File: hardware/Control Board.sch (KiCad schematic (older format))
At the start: 38 parts, among them J1 Conn_FTDI, J2 SOLAR, M1 Motor_DC, Q1 IRF7105PbF, Q2 BC817W, Q3 BC817W, Q4 IRF7105PbF, SW1 SW_Push, SW2 SW_Push, SW3 SW_Push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

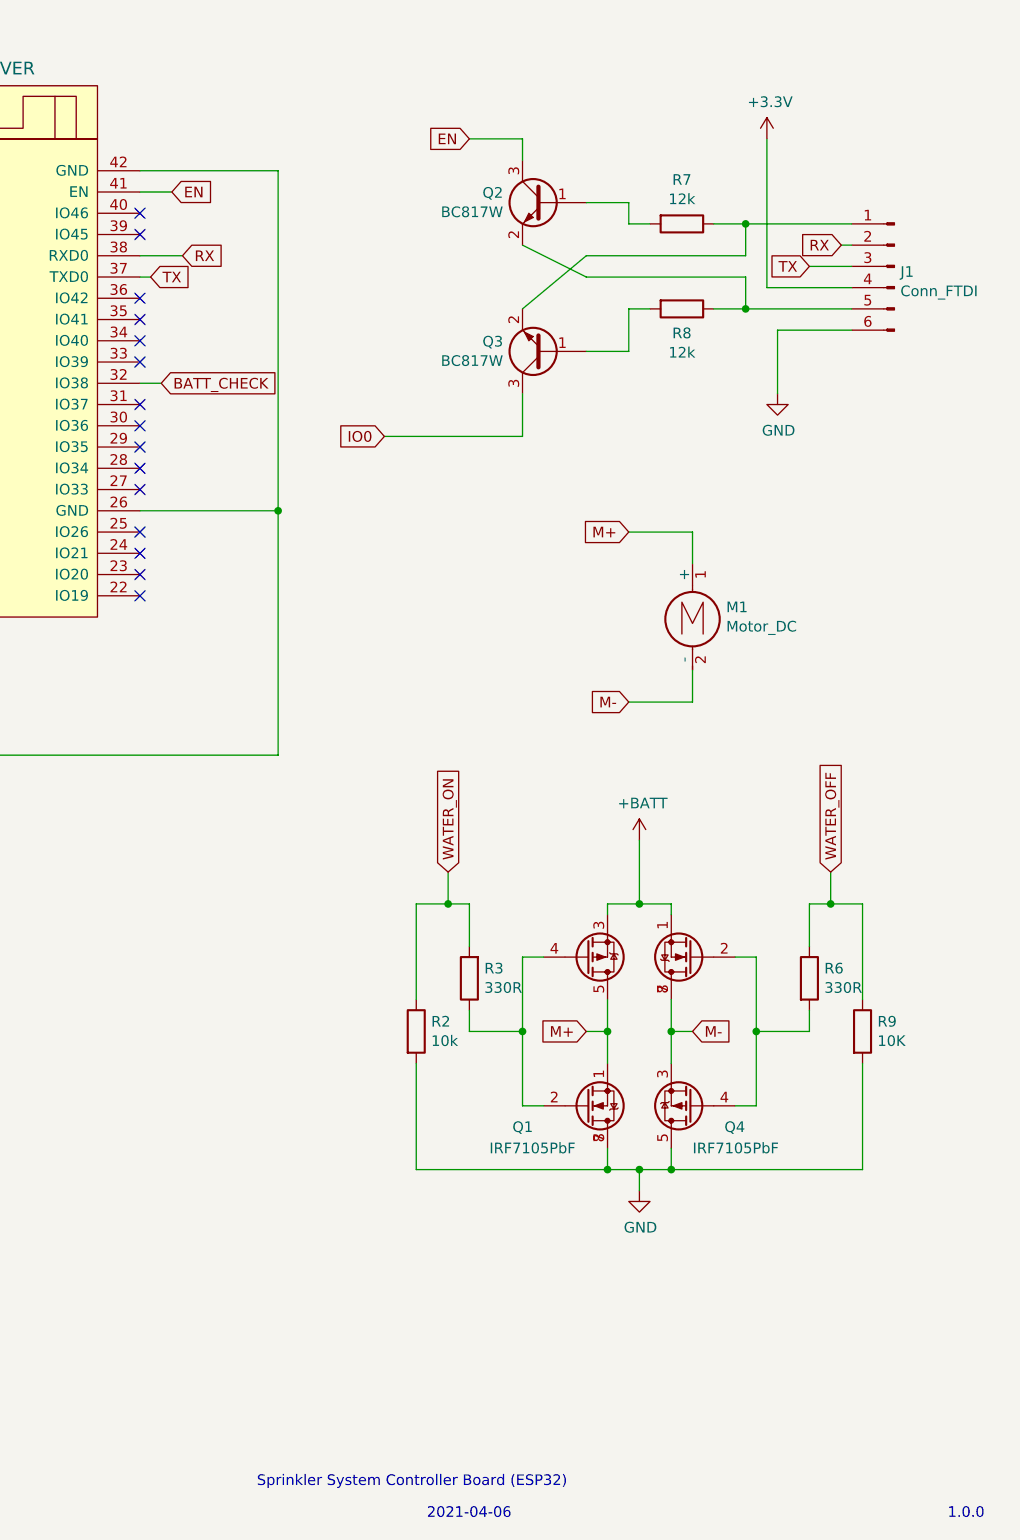
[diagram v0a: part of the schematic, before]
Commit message: Add pull up resistors on the auto programmer circuit, switch the RX and TX lines
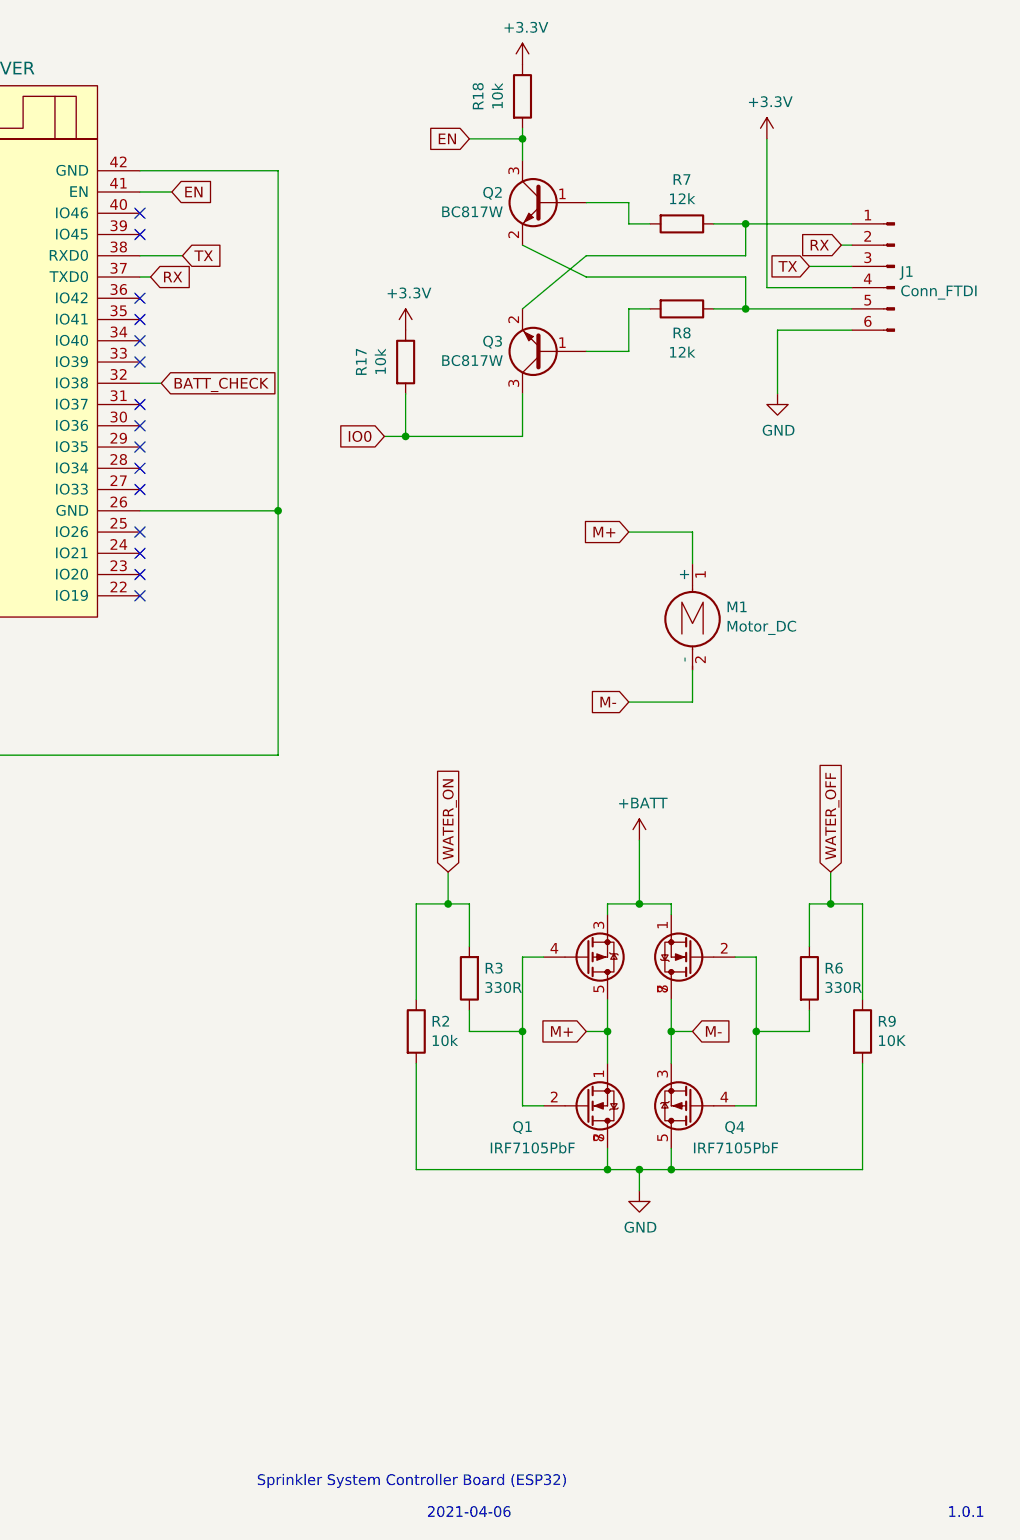
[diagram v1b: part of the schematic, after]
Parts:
- added R17, R18: 10k, Resistor_SMD:R_0402_1005Metric, symbol Device:R
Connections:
- net +3V3: now also R17.1, R18.1
- net EN: now also R18.2
- net IO0: now also R17.2
- net RX: now also U3.37 (TXD0); no longer U3.38 (RXD0)
- net TX: now also U3.38 (RXD0); no longer U3.37 (TXD0)
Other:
- note added: "1.0.1"
- note removed: "1.0.0\n"
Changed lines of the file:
@@
 Text Notes 7350 7500 0    50   ~ 0
 Sprinkler System Controller Board (ESP32)
-Text Notes 10600 7650 0    50   ~ 0
-1.0.0\n
 Text Notes 8150 7650 0    50   ~ 0
 2021-04-06
@@
 Text GLabel 4550 2400 0    50   Input ~ 0
 CHRG
-Text GLabel 7000 1700 2    50   Input ~ 0
-RX
 Wire Wire Line
 	6800 1700 7000 1700
@@
 Wire Wire Line
 	800  4350 800  4450
-Wire Wire Line
-	7950 2550 8600 2550
+Text Notes 10600 7650 0    50   ~ 0
+1.0.1
 Text GLabel 6850 1800 2    50   Input ~ 0
+RX
+Text GLabel 7000 1700 2    50   Input ~ 0
 TX
+Connection ~ 8600 1150
+Wire Wire Line
+	8600 1100 8600 1150
+$Comp
+L Device:R R18
+U 1 1 606B8BF0
+P 8600 950
+F 0 "R18" V 8393 950 50  0000 C CNN
+F 1 "10k" V 8484 950 50  0000 C CNN
+F 2 "Resistor_SMD:R_0402_1005Metric" V 8530 950 50  0001 C CNN
+F 3 "~" H 8600 950 50  0001 C CNN
+	1    8600 950
+	1    0    0    -1
+$EndComp
+$Comp
+L power:+3.3V #PWR0109
+U 1 1 606D7C17
+P 8600 800
+F 0 "#PWR0109" H 8600 650 50  0001 C CNN
+F 1 "+3.3V" H 8615 973 50  0000 C CNN
+F 2 "" H 8600 800 50  0001 C CNN
+F 3 "" H 8600 800 50  0001 C CNN
+	1    8600 800
+	1    0    0    -1
+$EndComp
+$Comp
+L power:+3.3V #PWR0110
+U 1 1 60726C87
+P 8050 2050
+F 0 "#PWR0110" H 8050 1900 50  0001 C CNN
+F 1 "+3.3V" H 8065 2223 50  0000 C CNN
+F 2 "" H 8050 2050 50  0001 C CNN
+F 3 "" H 8050 2050 50  0001 C CNN
+	1    8050 2050
+	1    0    0    -1
+$EndComp
+$Comp
+L Device:R R17
+U 1 1 60726C80
+P 8050 2200
+F 0 "R17" V 7843 2200 50  0000 C CNN
+F 1 "10k" V 7934 2200 50  0000 C CNN
+F 2 "Resistor_SMD:R_0402_1005Metric" V 7980 2200 50  0001 C CNN
+F 3 "~" H 8050 2200 50  0001 C CNN
+	1    8050 2200
+	1    0    0    -1
+$EndComp
+Wire Wire Line
+	8050 2550 8600 2550
+Wire Wire Line
+	7950 2550 8050 2550
+Connection ~ 8050 2550
+Wire Wire Line
+	8050 2350 8050 2550
 $EndSCHEMATC

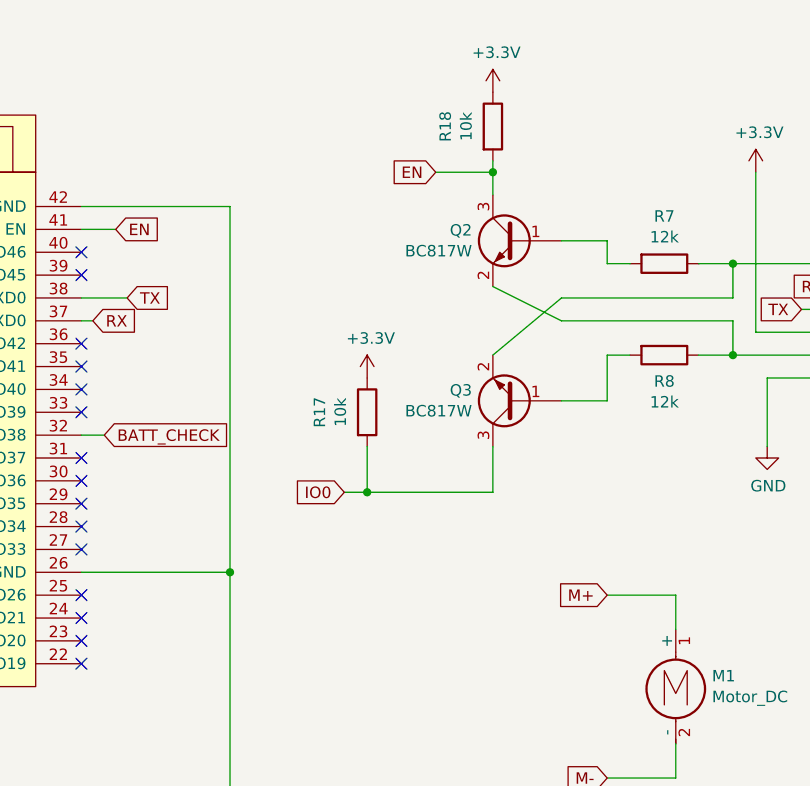
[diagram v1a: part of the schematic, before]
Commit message: RX and TX were crossing over, adding spots for capacitors on EN and IO0
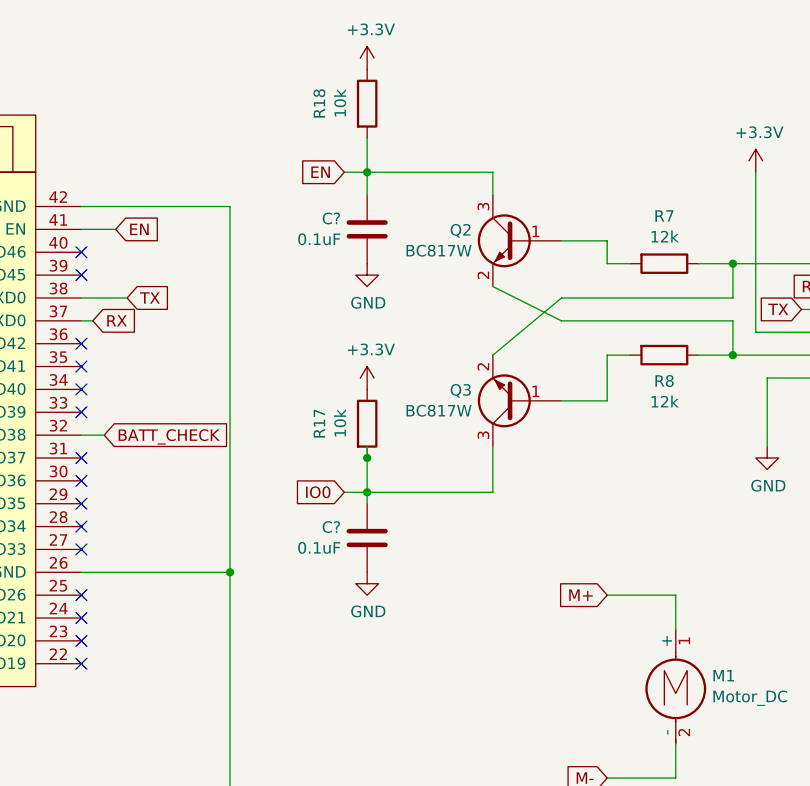
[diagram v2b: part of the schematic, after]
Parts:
- added C? (x2): 0.1uF, Capacitor_SMD:C_0402_1005Metric, symbol Device:C
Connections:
- net EN: now also C?.1
- net GND: now also C?.2, C?.2
- net IO0: now also C?.1
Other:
- moved on the sheet: R17, R18
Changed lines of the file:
@@
 Wire Wire Line
 	8900 1800 8600 1650
-Text GLabel 8350 1150 0    50   Input ~ 0
+Text GLabel 7950 1150 0    50   Input ~ 0
 EN
 Text GLabel 7950 2550 0    50   Input ~ 0
@@
 	9950 1750 10150 1750
 Wire Wire Line
-	8350 1150 8600 1150
+	7950 1150 8050 1150
 Wire Wire Line
 	8600 1150 8600 1250
@@
 Text GLabel 7000 1700 2    50   Input ~ 0
 TX
-Connection ~ 8600 1150
-Wire Wire Line
-	8600 1100 8600 1150
 $Comp
 L Device:R R18
 U 1 1 606B8BF0
-P 8600 950
-F 0 "R18" V 8393 950 50  0000 C CNN
-F 1 "10k" V 8484 950 50  0000 C CNN
-F 2 "Resistor_SMD:R_0402_1005Metric" V 8530 950 50  0001 C CNN
-F 3 "~" H 8600 950 50  0001 C CNN
-	1    8600 950
+P 8050 850
+F 0 "R18" V 7843 850 50  0000 C CNN
+F 1 "10k" V 7934 850 50  0000 C CNN
+F 2 "Resistor_SMD:R_0402_1005Metric" V 7980 850 50  0001 C CNN
+F 3 "~" H 8050 850 50  0001 C CNN
+	1    8050 850
 	1    0    0    -1
 $EndComp
@@
 L power:+3.3V #PWR0109
 U 1 1 606D7C17
-P 8600 800
-F 0 "#PWR0109" H 8600 650 50  0001 C CNN
-F 1 "+3.3V" H 8615 973 50  0000 C CNN
-F 2 "" H 8600 800 50  0001 C CNN
-F 3 "" H 8600 800 50  0001 C CNN
-	1    8600 800
+P 8050 700
+F 0 "#PWR0109" H 8050 550 50  0001 C CNN
+F 1 "+3.3V" H 8065 873 50  0000 C CNN
+F 2 "" H 8050 700 50  0001 C CNN
+F 3 "" H 8050 700 50  0001 C CNN
+	1    8050 700
 	1    0    0    -1
 $EndComp
@@
 L power:+3.3V #PWR0110
 U 1 1 60726C87
-P 8050 2050
-F 0 "#PWR0110" H 8050 1900 50  0001 C CNN
-F 1 "+3.3V" H 8065 2223 50  0000 C CNN
-F 2 "" H 8050 2050 50  0001 C CNN
-F 3 "" H 8050 2050 50  0001 C CNN
-	1    8050 2050
+P 8050 2100
+F 0 "#PWR0110" H 8050 1950 50  0001 C CNN
+F 1 "+3.3V" H 8065 2273 50  0000 C CNN
+F 2 "" H 8050 2100 50  0001 C CNN
+F 3 "" H 8050 2100 50  0001 C CNN
+	1    8050 2100
 	1    0    0    -1
 $EndComp
@@
 L Device:R R17
 U 1 1 60726C80
-P 8050 2200
-F 0 "R17" V 7843 2200 50  0000 C CNN
-F 1 "10k" V 7934 2200 50  0000 C CNN
-F 2 "Resistor_SMD:R_0402_1005Metric" V 7980 2200 50  0001 C CNN
-F 3 "~" H 8050 2200 50  0001 C CNN
-	1    8050 2200
+P 8050 2250
+F 0 "R17" V 7843 2250 50  0000 C CNN
+F 1 "10k" V 7934 2250 50  0000 C CNN
+F 2 "Resistor_SMD:R_0402_1005Metric" V 7980 2250 50  0001 C CNN
+F 3 "~" H 8050 2250 50  0001 C CNN
+	1    8050 2250
 	1    0    0    -1
 $EndComp
@@
 Connection ~ 8050 2550
 Wire Wire Line
-	8050 2350 8050 2550
+	8050 2350 8050 2400
+$Comp
+L Device:C C?
+U 1 1 6072C4CA
+P 8050 2750
+F 0 "C?" H 7936 2796 50  0000 R CNN
+F 1 "0.1uF" H 7936 2705 50  0000 R CNN
+F 2 "Capacitor_SMD:C_0402_1005Metric" H 8088 2600 50  0001 C CNN
+F 3 "~" H 8050 2750 50  0001 C CNN
+	1    8050 2750
+	1    0    0    -1
+$EndComp
+$Comp
+L power:GND #PWR?
+U 1 1 607982DE
+P 8050 2900
+F 0 "#PWR?" H 8050 2650 50  0001 C CNN
+F 1 "GND" H 8055 2727 50  0000 C CNN
+F 2 "" H 8050 2900 50  0001 C CNN
+F 3 "" H 8050 2900 50  0001 C CNN
+	1    8050 2900
+	1    0    0    -1
+$EndComp
+Wire Wire Line
+	8050 2550 8050 2600
+$Comp
+L Device:C C?
+U 1 1 608072F7
+P 8050 1400
+F 0 "C?" H 7936 1446 50  0000 R CNN
+F 1 "0.1uF" H 7936 1355 50  0000 R CNN
+F 2 "Capacitor_SMD:C_0402_1005Metric" H 8088 1250 50  0001 C CNN
+F 3 "~" H 8050 1400 50  0001 C CNN
+	1    8050 1400
+	1    0    0    -1
+$EndComp
+$Comp
+L power:GND #PWR?
+U 1 1 608072FD
+P 8050 1550
+F 0 "#PWR?" H 8050 1300 50  0001 C CNN
+F 1 "GND" H 8055 1377 50  0000 C CNN
+F 2 "" H 8050 1550 50  0001 C CNN
+F 3 "" H 8050 1550 50  0001 C CNN
+	1    8050 1550
+	1    0    0    -1
+$EndComp
+Wire Wire Line
+	8050 1000 8050 1150
+Connection ~ 8050 1150
+Wire Wire Line
+	8050 1150 8600 1150
+Wire Wire Line
+	8050 1150 8050 1250
+Connection ~ 8050 2400
+Wire Wire Line
+	8050 2400 8050 2550
 $EndSCHEMATC

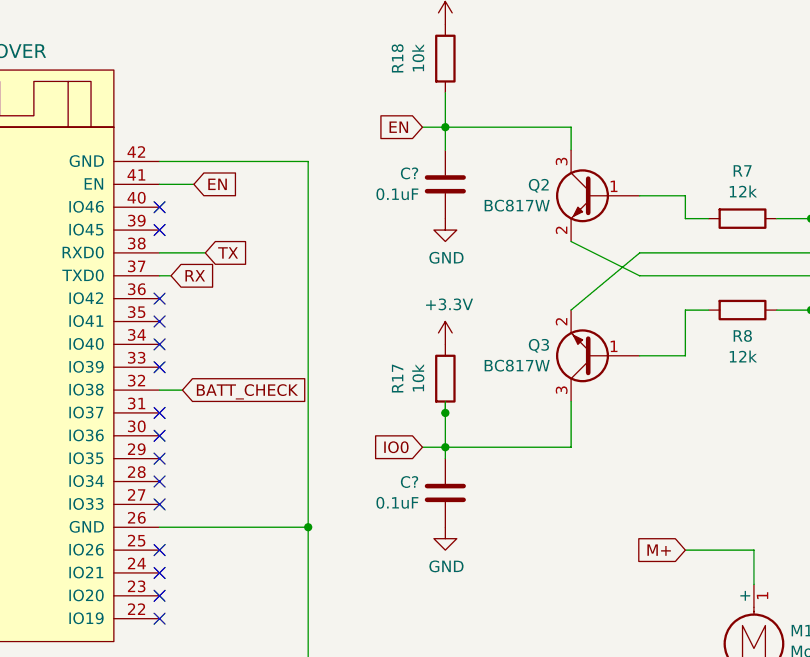
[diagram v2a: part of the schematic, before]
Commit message: RX and TX were crossing over, adding spots for capacitors on EN and IO0
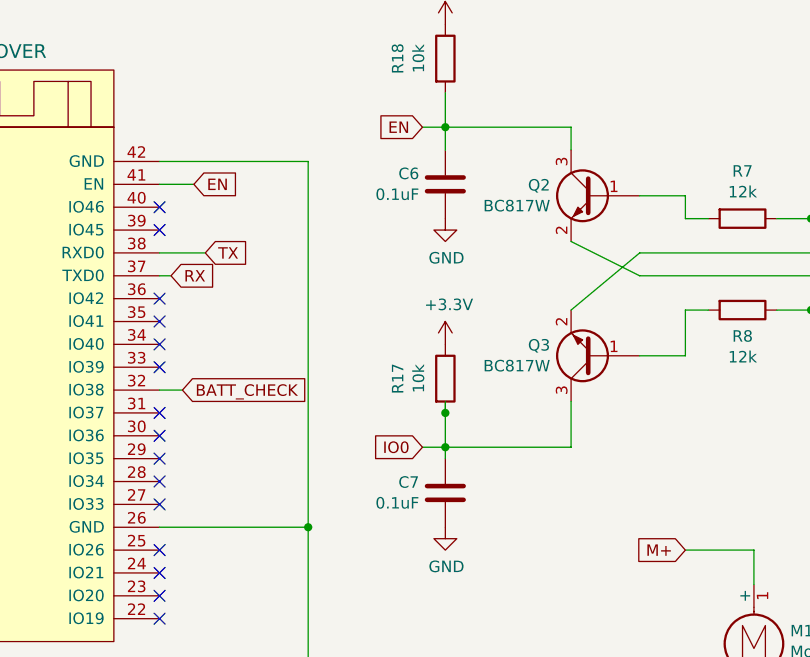
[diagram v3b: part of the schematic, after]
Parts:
- gave numbers to parts that had none: 2
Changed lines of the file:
@@
 	2750 6100 2900 6100
-Wire Wire Line
-	2650 4450 2750 4450
 Wire Wire Line
 	4050 4450 4050 5200
@@
 	2750 4350 2750 4450
 Connection ~ 2750 4450
-Wire Wire Line
-	2750 4450 4050 4450
 Wire Wire Line
 	2050 6100 2750 6100
@@
 	8050 2350 8050 2400
 $Comp
-L Device:C C?
+L Device:C C7
 U 1 1 6072C4CA
 P 8050 2750
-F 0 "C?" H 7936 2796 50  0000 R CNN
+F 0 "C7" H 7936 2796 50  0000 R CNN
 F 1 "0.1uF" H 7936 2705 50  0000 R CNN
 F 2 "Capacitor_SMD:C_0402_1005Metric" H 8088 2600 50  0001 C CNN
@@
 $EndComp
 $Comp
-L power:GND #PWR?
+L power:GND #PWR0113
 U 1 1 607982DE
 P 8050 2900
-F 0 "#PWR?" H 8050 2650 50  0001 C CNN
+F 0 "#PWR0113" H 8050 2650 50  0001 C CNN
 F 1 "GND" H 8055 2727 50  0000 C CNN
 F 2 "" H 8050 2900 50  0001 C CNN
@@
 	8050 2550 8050 2600
 $Comp
-L Device:C C?
+L Device:C C6
 U 1 1 608072F7
 P 8050 1400
-F 0 "C?" H 7936 1446 50  0000 R CNN
+F 0 "C6" H 7936 1446 50  0000 R CNN
 F 1 "0.1uF" H 7936 1355 50  0000 R CNN
 F 2 "Capacitor_SMD:C_0402_1005Metric" H 8088 1250 50  0001 C CNN
@@
 $EndComp
 $Comp
-L power:GND #PWR?
+L power:GND #PWR0114
 U 1 1 608072FD
 P 8050 1550
-F 0 "#PWR?" H 8050 1300 50  0001 C CNN
+F 0 "#PWR0114" H 8050 1300 50  0001 C CNN
 F 1 "GND" H 8055 1377 50  0000 C CNN
 F 2 "" H 8050 1550 50  0001 C CNN
@@
 Wire Wire Line
 	8050 2400 8050 2550
+Wire Wire Line
+	2650 4450 2750 4450
+Wire Wire Line
+	2750 4450 4050 4450
 $EndSCHEMATC
